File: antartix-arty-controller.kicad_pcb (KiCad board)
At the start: 4 copper layers, 173.5 x 40 mm, 131 parts, among them IC1 FT2232D, IC2 TPD8S009DSMR, IC3 TPD8S009DSMR, J1 QTE-020-04-L-D-A, J2 0022232041, J3 614004185023, J4 WE_629105150521, J5 614004185023, J6 614004185023, J7 QTE-020-04-L-D-A, J8 685119134923, J9 685119134923, U1 PCT2075GVX, U2 PAC1934T-I_JQ, U3 USB2514B-I_M2, U4 TPS2024DR, U5 TPS2024DR, U6 TPS2024DR, Y1 7C-24.000MBB-T, Y2 MQ-6.000-12-30_30_

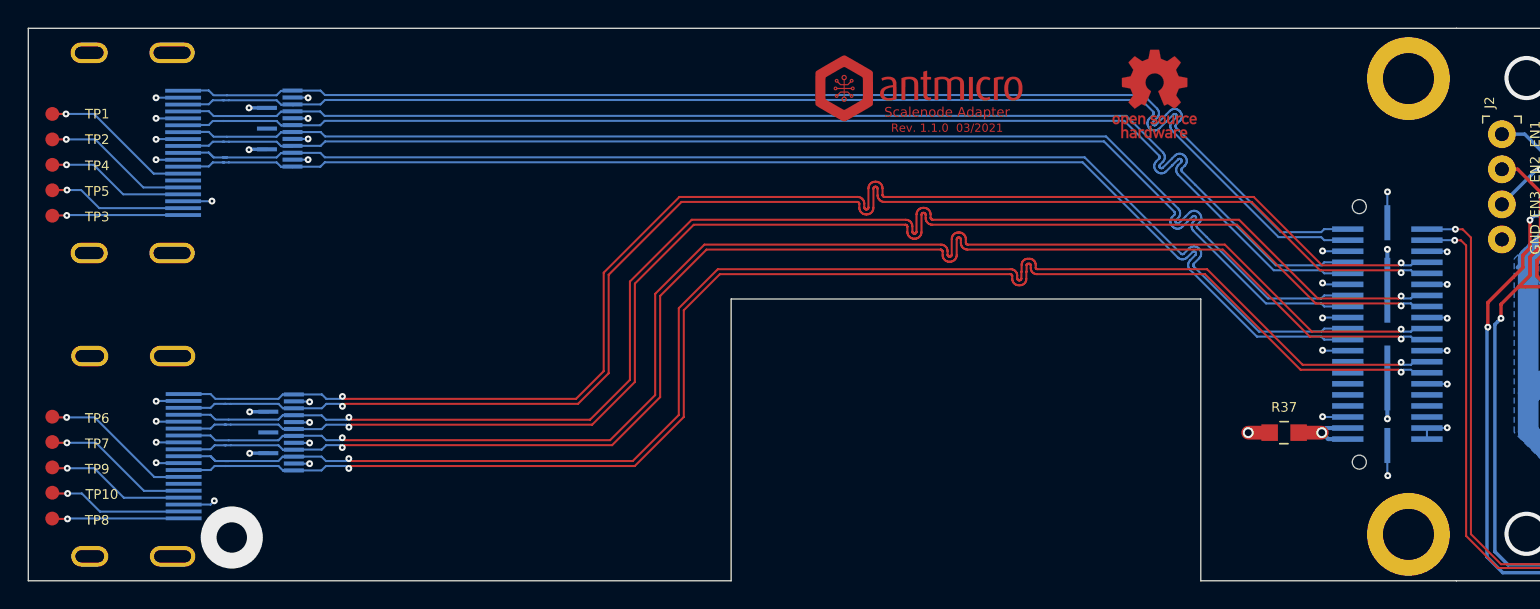
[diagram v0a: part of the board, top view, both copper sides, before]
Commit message: Add component placement
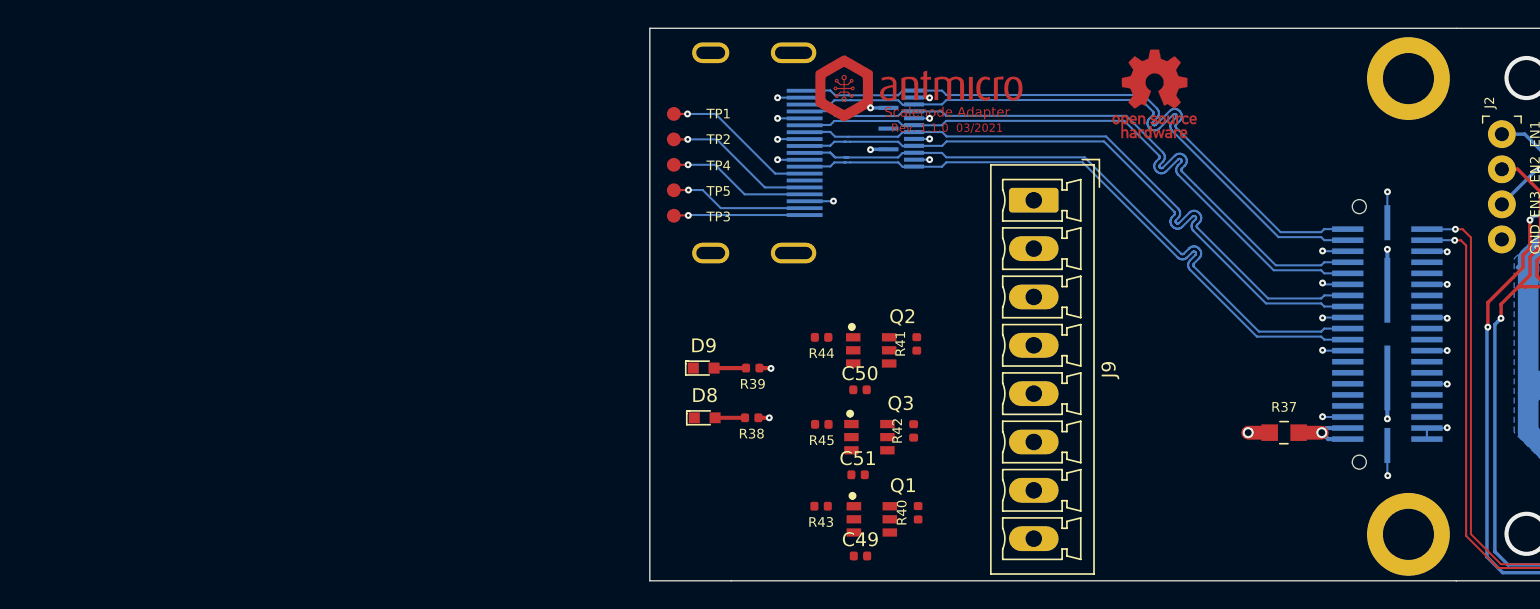
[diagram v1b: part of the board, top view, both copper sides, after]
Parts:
- removed IC3: TPD8S009DSMR, antmicro-footprints:R-PDSO-N15
- removed TP10, TP6, TP7, TP8, TP9: TP_SMD1MM, antmicro-footprints:Testpoint_smd_1mm
- added C49: C_10n_0402, antmicro-footprints:0402-cap, F.Cu at (124.8, 110.7)
- added C50: C_10n_0402, antmicro-footprints:0402-cap, F.Cu at (124.7, 98.7)
- added C51: C_10n_0402, antmicro-footprints:0402-cap, F.Cu at (124.6, 104.8)
- added D8: LG_L29K-G2J1-24-Z, antartix-arty-controller-footprints:LED_0603, F.Cu at (113.5, 100.7)
- added D9: LG_L29K-G2J1-24-Z, antartix-arty-controller-footprints:LED_0603, F.Cu at (113.4, 97.1)
- added Q1: FDC6330L, antmicro-footprints:FDC6330L, F.Cu at (125.6, 108.1)
- added Q2: FDC6330L, antmicro-footprints:FDC6330L, F.Cu at (125.5, 95.8)
- added Q3: FDC6330L, antmicro-footprints:FDC6330L, F.Cu at (125.4, 102.1)
- added R38: R_470R_0402, antartix-arty-controller-footprints:0402-res, F.Cu at (116.9, 100.7)
- added R39: R_470R_0402, antartix-arty-controller-footprints:0402-res, F.Cu at (117.0, 97.1)
- added R40: R_1k_0402, antmicro-footprints:0402-res, F.Cu at (128.9, 107.6)
- added R41: R_1k_0402, antmicro-footprints:0402-res, F.Cu at (128.8, 95.4)
- added R42: R_1k_0402, antmicro-footprints:0402-res, F.Cu at (128.6, 101.7)
- added R43: R_100R_0402, antmicro-footprints:0402-res, F.Cu at (121.9, 107.1)
- added R44: R_100R_0402, antmicro-footprints:0402-res, F.Cu at (121.9, 94.9)
- added R45: R_100R_0402, antmicro-footprints:0402-res, F.Cu at (122.0, 101.2)
- J9: value 685119134923 -> Screw_Terminal_01x08; footprint antmicro-footprints:HDMI_A_Female_685119134923 -> Connector_Phoenix_MC:PhoenixContact_MCV_1,5_8-G-3.5_1x08_P3.50mm_Vertical; moved to F.Cu
- moved J9 65.5 mm to (137.3, 85.0)
- moved IC2 45.0 mm to (126.9, 79.8)
- moved J8 45.0 mm to (119.4, 81.5)
- moved TP1 45.0 mm to (111.3, 78.8)
- moved TP2 45.0 mm to (111.3, 80.6)
- moved TP3 45.0 mm to (111.3, 86.1)
- moved TP4 45.0 mm to (111.3, 82.4)
- moved TP5 45.0 mm to (111.3, 84.3)
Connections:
- net /antartix usb adapter/USB1_EN renamed USB1_EN
- net /antartix usb adapter/USB2_EN renamed USB2_EN
- net /antartix usb adapter/USB3_EN renamed USB3_EN
- J9 pad 1: HDMI1_D2_P -> /Aux power supply/GND_IN
- J9 pad 2: GND -> /Aux power supply/GND3
- J9 pad 3: HDMI1_D2_N -> /Aux power supply/VCC_9V_IN
- J9 pad 4: HDMI1_D1_P -> /Aux power supply/VCC_9V_OUT_3
- J9 pad 5: GND -> /Aux power supply/VCC_9V_OUT_2
- J9 pad 6: HDMI1_D1_N -> /Aux power supply/VCC_9V_OUT_1
- J9 pad 7: HDMI1_D0_P -> /Aux power supply/GND2
- J9 pad 8: GND -> /Aux power supply/GND1
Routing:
- net HDMI1_CK_P: track 107.8 -> 0.00 mm, vias 2 -> 0
- net HDMI1_CK_N: track 107.2 -> 0.00 mm, vias 2 -> 0
- net HDMI1_D1_N: track 106.4 -> 0.00 mm, vias 2 -> 0
- net HDMI1_D0_N: track 106.4 -> 0.00 mm, vias 2 -> 0
- net HDMI1_D2_N: track 106.3 -> 0.00 mm, vias 2 -> 0
- net HDMI1_D0_P: track 106.3 -> 0.00 mm, vias 2 -> 0
- net HDMI1_D1_P: track 106.2 -> 0.00 mm, vias 2 -> 0
- net HDMI1_D2_P: track 106.2 -> 0.00 mm, vias 2 -> 0
- net HDMI0_D2_N: track 92.4 -> 47.4 mm
- net HDMI0_D1_N: track 92.4 -> 47.4 mm
- net HDMI0_D0_N: track 92.4 -> 47.4 mm
- net HDMI0_CK_N: track 92.8 -> 47.8 mm
- net HDMI0_D0_P: track 92.3 -> 47.3 mm
- net HDMI0_D2_P: track 92.2 -> 47.2 mm
- net HDMI0_D1_P: track 92.2 -> 47.2 mm
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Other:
- board size 173.5 x 40 mm -> 128.5 x 40 mm

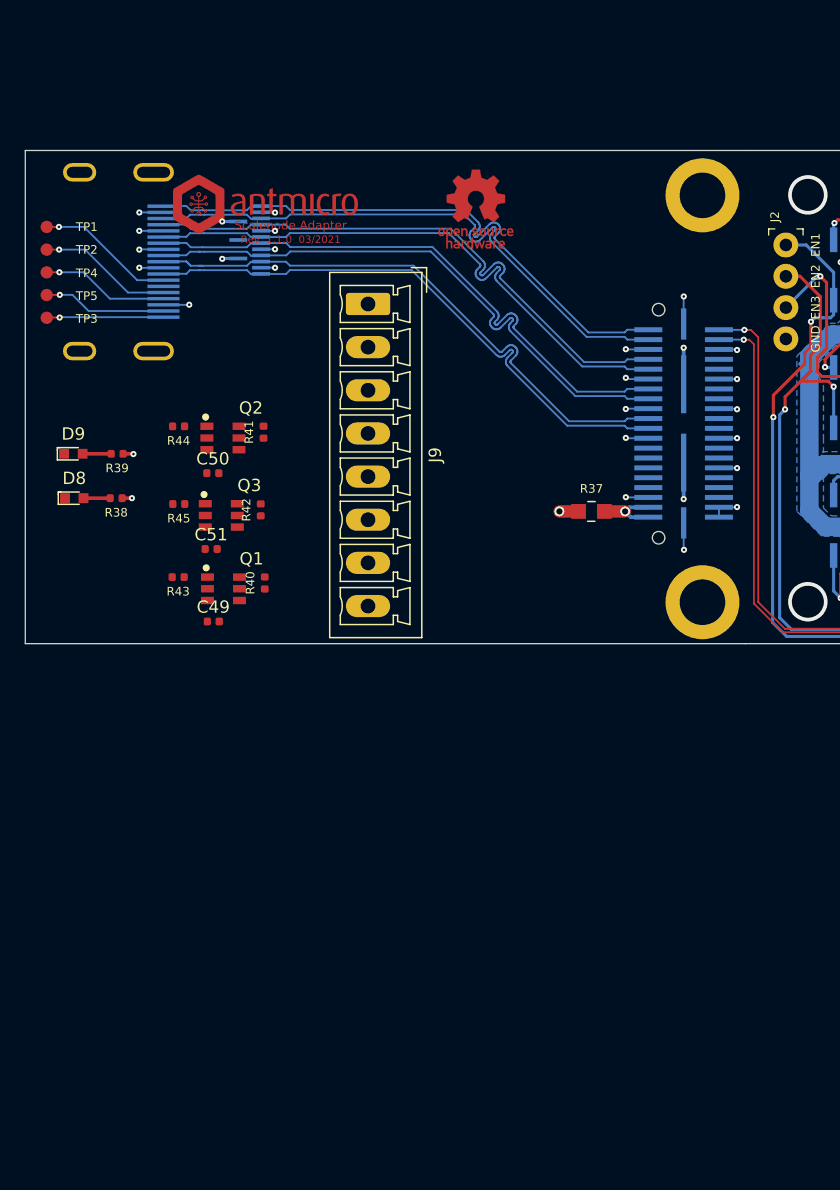
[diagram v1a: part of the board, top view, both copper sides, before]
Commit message: Reduce board size, update connector placement
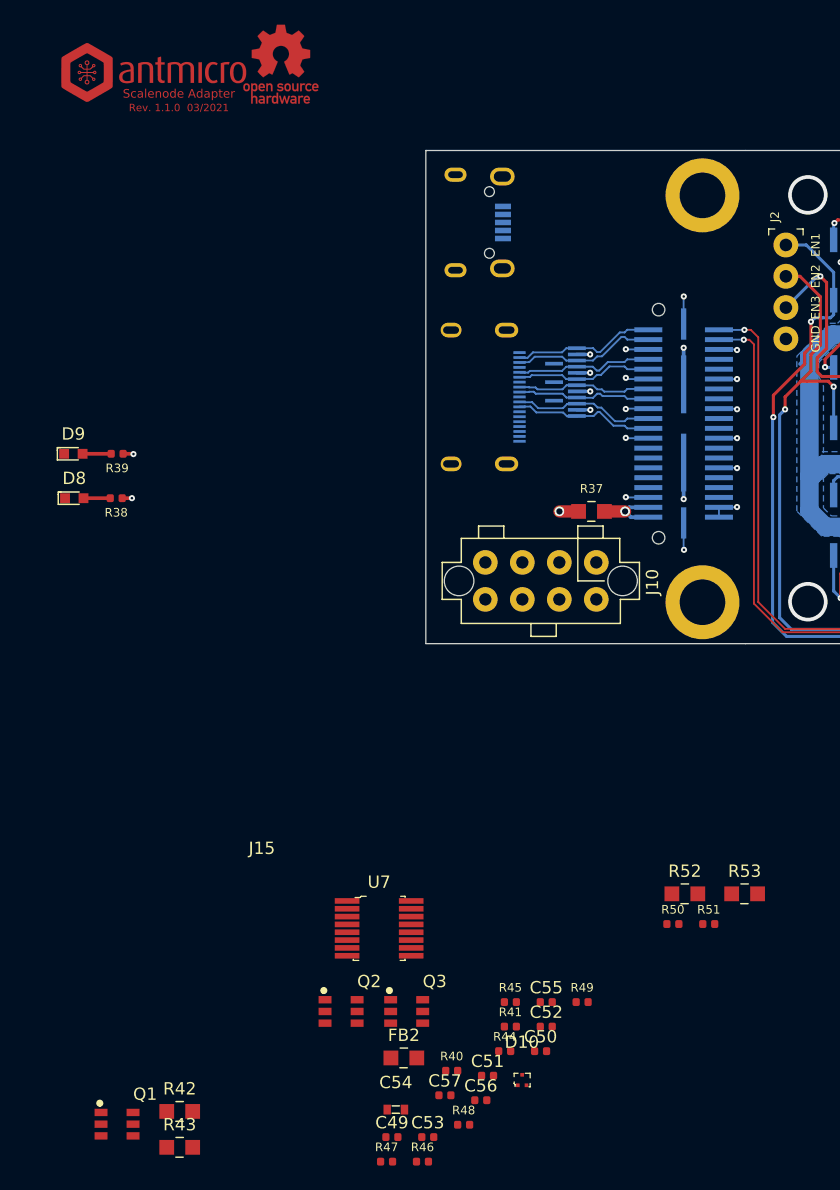
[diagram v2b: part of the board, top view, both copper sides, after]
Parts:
- removed TP1, TP2, TP3, TP4, TP5: TP_SMD1MM, antmicro-footprints:Testpoint_smd_1mm
- added C52: C_1u_0402, antmicro-footprints:0402-cap, F.Cu at (151.8, 143.6)
- added C53: C_100n_0402, antartix-arty-controller-footprints:0402-cap, F.Cu at (142.2, 152.5)
- added C54: C_22u_0603, antmicro-footprints:0603-cap, F.Cu at (139.6, 150.3)
- added C55: C_470p_0402, antmicro-footprints:0402-cap, F.Cu at (151.8, 141.6)
- added C56: C_470p_0402, antmicro-footprints:0402-cap, F.Cu at (146.5, 149.5)
- added C57: C_470p_0402, antmicro-footprints:0402-cap, F.Cu at (143.5, 149.1)
- added D10: TPD2E009, antartix-arty-controller-footprints:SOT-3, F.Cu at (149.8, 147.9)
- added FB2: BLM21SP111BH1, antartix-arty-controller-footprints:0805-res, F.Cu at (140.2, 146.1)
- added J10: 3-794680-8, antmicro-footprints:3-794680-8, F.Cu at (155.8, 105.9)
- added J11: 1-794610-1, antmicro-footprints:1-794610-1, F.Cu at (145.2, 141.3)
- added J12: 1-794610-1, antmicro-footprints:1-794610-1, F.Cu at (130.8, 153.7)
- added J13: 1-794610-1, antmicro-footprints:1-794610-1, F.Cu at (116.3, 154.5)
- added J14: 1-794610-1, antmicro-footprints:1-794610-1, F.Cu at (126.5, 153.7)
- added J15: 3-794617-8, antmicro-footprints:3-794617-8, F.Cu at (127.1, 133.7)
- added J16: 1-794610-1, antmicro-footprints:1-794610-1, F.Cu at (145.2, 142.8)
- added J17: 1-794610-1, antmicro-footprints:1-794610-1, F.Cu at (144.7, 145.4)
- added J18: 1-794610-1, antmicro-footprints:1-794610-1, F.Cu at (135.1, 153.7)
- added J19: 1-794610-1, antmicro-footprints:1-794610-1, F.Cu at (139.8, 148.3)
- added R46: R_47k_0402, antartix-arty-controller-footprints:0402-res, F.Cu at (141.7, 154.5)
- added R47: R_1k_0402, antmicro-footprints:0402-res, F.Cu at (138.8, 154.5)
- added R48: R_1k_0402, antmicro-footprints:0402-res, F.Cu at (145.1, 151.5)
- added R49: R_1k_0402, antmicro-footprints:0402-res, F.Cu at (154.7, 141.6)
- added R50: R_47k_0402, antartix-arty-controller-footprints:0402-res, F.Cu at (162.0, 135.2)
- added R51: R_47k_0402, antartix-arty-controller-footprints:0402-res, F.Cu at (164.9, 135.2)
- added R52: R_0R_0805, antmicro-footprints:0805-res, F.Cu at (163.0, 132.8)
- added R53: R_0R_0805, antmicro-footprints:0805-res, F.Cu at (167.9, 132.8)
- added U7: FT230XS-R, antmicro-footprints:SSOP-16_W3.90mm, F.Cu at (138.2, 135.6)
- C49, C50: value C_10n_0402 -> C_100n_0402; footprint antmicro-footprints:0402-cap -> antartix-arty-controller-footprints:0402-cap
- C51: value C_10n_0402 -> C_1u_0402
- J8: value 685119134923 -> WE_629105150521; footprint antmicro-footprints:HDMI_A_Female_685119134923 -> antartix-arty-controller-footprints:USB_Micro_B_Female_629105150521
- J9: value Screw_Terminal_01x08 -> WE_685119136923; footprint Connector_Phoenix_MC:PhoenixContact_MCV_1,5_8-G-3.5_1x08_P3.50mm_Vertical -> antmicro-footprints:WE_685119136923; moved to B.Cu
- R40: value R_1k_0402 -> R_4k7_0402; footprint antmicro-footprints:0402-res -> antartix-arty-controller-footprints:0402-res
- R41: value R_1k_0402 -> R_10k_0402; footprint antmicro-footprints:0402-res -> antartix-arty-controller-footprints:0402-res
- R42: value R_1k_0402 -> R_0R_0805; footprint antmicro-footprints:0402-res -> antmicro-footprints:0805-res
- R43: value R_100R_0402 -> R_0R_0805; footprint antmicro-footprints:0402-res -> antmicro-footprints:0805-res
- R44, R45: value R_100R_0402 -> R_47k_0402; footprint antmicro-footprints:0402-res -> antartix-arty-controller-footprints:0402-res
- moved R44 57.2 mm to (148.4, 145.6), turned to 0 degrees
- moved C50 53.9 mm to (151.3, 145.6)
- moved R41 52.2 mm to (148.9, 143.6), turned to 0 degrees
- moved R42 49.2 mm to (122.0, 150.4), turned to 0 degrees
- moved R45 48.5 mm to (148.9, 141.6), turned to 0 degrees
- moved C51 48.2 mm to (147.0, 147.5)
- moved Q2 47.5 mm to (135.1, 142.3)
- moved R43 46.3 mm to (122.0, 153.4), turned to 0 degrees
- moved Q1 44.3 mm to (117.0, 151.5)
- moved C49 44.3 mm to (139.2, 152.5)
- moved Q3 42.9 mm to (140.4, 142.3)
- moved R40 42.4 mm to (144.1, 147.1), turned to 0 degrees
- moved IC2 28.1 mm to (152.5, 91.3)
- moved J8 27.1 mm to (146.4, 78.3), turned to 90 degrees
- moved N2 19.7 mm to (130.2, 65.5)
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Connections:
- net /antartix usb adapter/USB_D_CON_N renamed /antartix usb adapter/USB_ALT_UP_N
- net /antartix usb adapter/USB_D_CON_P renamed /antartix usb adapter/USB_ALT_UP_P
- C49 pad 1: /Aux power supply/VCC_9V_OUT_1 -> Net-(C49-Pad1)
- C49 pad 2: Net-(C49-Pad2) -> GND
- C50 pad 1: /Aux power supply/VCC_9V_OUT_3 -> VCC5V0
- C50 pad 2: Net-(C50-Pad2) -> GND
- C51 pad 1: /Aux power supply/VCC_9V_OUT_2 -> VCC5V0
- C51 pad 2: Net-(C51-Pad2) -> GND
- D8 pad 1: Net-(D8-Pad1) -> LED0
- D9 pad 1: Net-(D9-Pad1) -> LED1
- J1 pad 25: /antartix usb adapter/~PWRDN -> LED0
- J1 pad 27: /antartix usb adapter/SLOW_~ALERT -> LED1
- J8 pad 1: HDMI0_D2_P -> Net-(J8-Pad1)
- J8 pad 2: GND -> /antartix hdmi adapter/USB_CON_N
- J8 pad 3: HDMI0_D2_N -> /antartix hdmi adapter/USB_CON_P
- J8 pad 4: HDMI0_D1_P -> Net-(J8-Pad4)
- J8 pad 6: HDMI0_D1_N -> GND
- J9 pad 1: /Aux power supply/GND_IN -> GND
- J9 pad 2: /Aux power supply/GND3 -> HDMI0_D2_P
- J9 pad 3: /Aux power supply/VCC_9V_IN -> HDMI0_D2_N
- J9 pad 4: /Aux power supply/VCC_9V_OUT_3 -> GND
- J9 pad 5: /Aux power supply/VCC_9V_OUT_2 -> HDMI0_D1_P
- J9 pad 6: /Aux power supply/VCC_9V_OUT_1 -> HDMI0_D1_N
- J9 pad 7: /Aux power supply/GND2 -> GND
- J9 pad 8: /Aux power supply/GND1 -> HDMI0_D0_P
- Q1 pad 2: /Aux power supply/VCC_9V_OUT_1 -> /antartix hdmi adapter/VCC_9V_OUT_1
- Q1 pad 3: /Aux power supply/VCC_9V_OUT_1 -> /antartix hdmi adapter/VCC_9V_OUT_1
- Q1 pad 4: USB1_EN -> /antartix hdmi adapter/VCC_9V_IN
- Q1 pad 5: Net-(Q1-Pad5) -> USB1_EN
- Q1 pad 6: Net-(C49-Pad2) -> Net-(C55-Pad2)
- Q2 pad 2: /Aux power supply/VCC_9V_OUT_3 -> /antartix hdmi adapter/VCC_9V_OUT_2
- Q2 pad 3: /Aux power supply/VCC_9V_OUT_3 -> /antartix hdmi adapter/VCC_9V_OUT_2
- Q2 pad 4: USB3_EN -> /antartix hdmi adapter/VCC_9V_IN
- Q2 pad 5: Net-(Q2-Pad5) -> USB2_EN
- Q2 pad 6: Net-(C50-Pad2) -> Net-(C56-Pad2)
- Q3 pad 2: /Aux power supply/VCC_9V_OUT_2 -> /antartix hdmi adapter/VCC_9V_OUT_3
- Q3 pad 3: /Aux power supply/VCC_9V_OUT_2 -> /antartix hdmi adapter/VCC_9V_OUT_3
- Q3 pad 4: USB2_EN -> /antartix hdmi adapter/VCC_9V_IN
- Q3 pad 5: Net-(Q3-Pad5) -> USB3_EN
- Q3 pad 6: Net-(C51-Pad2) -> Net-(C57-Pad2)
- R40 pad 1: USB1_EN -> Net-(J8-Pad1)
- R40 pad 2: Net-(C49-Pad2) -> Net-(R40-Pad2)
- R41 pad 1: USB3_EN -> Net-(R40-Pad2)
- R41 pad 2: Net-(C50-Pad2) -> GND
- R42 pad 1: USB2_EN -> Net-(R42-Pad1)
- R42 pad 2: Net-(C51-Pad2) -> RXD0
- R43 pad 1: Net-(Q1-Pad1) -> Net-(R43-Pad1)
- R43 pad 2: /Aux power supply/GND1 -> TXD0
- R44 pad 1: Net-(Q2-Pad1) -> /antartix hdmi adapter/VCC_9V_IN
- R44 pad 2: /Aux power supply/GND3 -> Net-(C55-Pad2)
- R45 pad 1: Net-(Q3-Pad1) -> /antartix hdmi adapter/VCC_9V_IN
- R45 pad 2: /Aux power supply/GND2 -> Net-(C56-Pad2)
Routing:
- net HDMI0_D0_N: track 47.4 -> 10.9 mm
- net HDMI0_CK_N: track 47.8 -> 11.5 mm
- net HDMI0_D0_P: track 47.3 -> 10.9 mm
- net HDMI0_CK_P: track 47.7 -> 11.4 mm
- net HDMI0_D1_N: track 47.4 -> 11.1 mm
- net HDMI0_D1_P: track 47.2 -> 11.1 mm
- net HDMI0_D2_N: track 47.4 -> 11.6 mm
- net HDMI0_D2_P: track 47.2 -> 11.6 mm
- net Net-(J8-Pad13): track 11.3 -> 0.00 mm, vias 1 -> 0
- net Net-(J8-Pad15): track 10.9 -> 0.00 mm, vias 1 -> 0
- net Net-(J8-Pad16): track 10.4 -> 0.00 mm, vias 1 -> 0
- net GND: track 104.5 -> 94.3 mm, vias 122 -> 117
- net Net-(J8-Pad18): track 10.0 -> 0.00 mm, vias 1 -> 0
- net Net-(J8-Pad19): track 9.49 -> 0.00 mm, vias 1 -> 0
- net VCC3V3: track 86.8 -> 84.1 mm, vias 24 -> 22
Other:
- board size 128.5 x 40 mm -> 96 x 40 mm
